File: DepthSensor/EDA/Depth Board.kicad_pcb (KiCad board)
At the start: 2 copper layers, 24 x 11.2 mm, 14 parts, among them J1 Conn_01x04, J2 Conn_01x03, J3 Screw_Terminal_01x03, J4 Conn_01x02, U1 ATmega328P-AU, Y1 8MHz

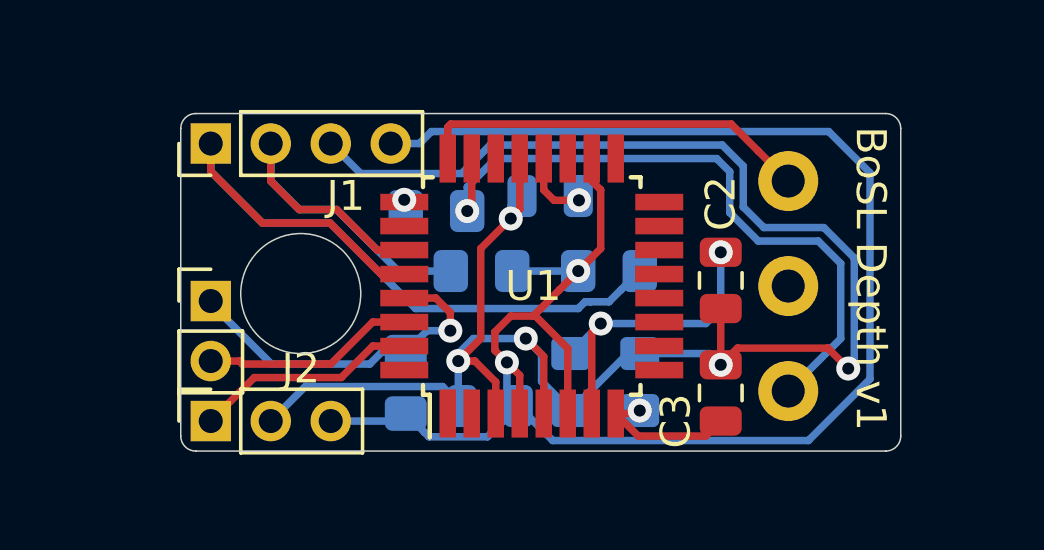
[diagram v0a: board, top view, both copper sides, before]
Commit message: added implementation of RS485 library
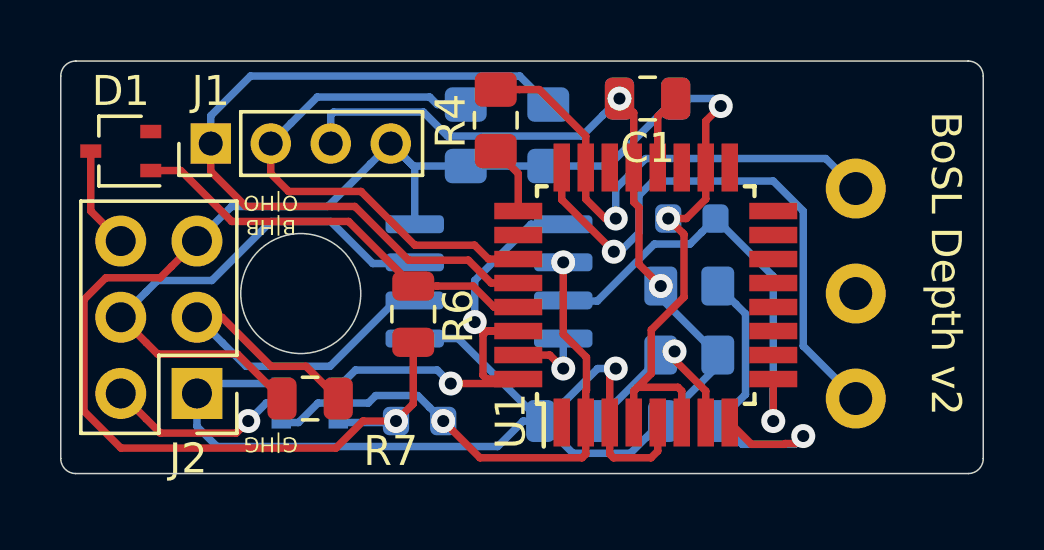
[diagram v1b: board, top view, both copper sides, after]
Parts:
- removed J4: Conn_01x02, SamacSys_Parts:Cable_2
- added D1: BAT54W, Package_TO_SOT_SMD:SOT-323_SC-70, F.Cu at (143.8, 95.0)
- added R5: 47 kΩ, Resistor_SMD:R_0603_1608Metric, B.Cu at (153.7, 104.0)
- added R6: 10 kΩ, Resistor_SMD:R_0805_2012Metric, F.Cu at (153.5, 100.4)
- added R7: 100 Ω, Resistor_SMD:R_0805_2012Metric, F.Cu at (150.1, 103.2)
- added U2: 74LVC1G126, Package_TO_SOT_SMD:SOT-353_SC-70-5, B.Cu at (150.1, 103.4)
- added U3: SN65HVD75, Package_SO:SOIC-8_3.9x4.9mm_P1.27mm, B.Cu at (156.0, 99.3)
- C1, R4: moved to F.Cu
- C2, C3: moved to B.Cu
- J2: value Conn_01x03 -> Conn_02x03_Odd_Even; footprint SamacSys_Parts:Cable -> Connector_PinHeader_2.54mm:PinHeader_2x03_P2.54mm_Vertical
- R1: value 10K -> 1 MΩ; footprint Resistor_SMD:R_0805_2012Metric_Pad1.15x1.40mm_HandSolder -> Resistor_SMD:R_0603_1608Metric
- moved C4 11.5 mm to (161.3, 93.2)
- moved R1 11.0 mm to (162.8, 97.2), turned to 180 degrees
- moved C2 6.90 mm to (158.7, 104.0), turned to 0 degrees
- moved R3 4.96 mm to (158.0, 94.5), turned to 90 degrees
- moved C1 4.60 mm to (161.3, 93.2)
- moved R2 4.56 mm to (155.2, 94.5), turned to 90 degrees
- moved U1 3.81 mm to (161.2, 99.8)
- moved R4 3.61 mm to (156.2, 94.0), turned to 90 degrees
- moved Y1 3.47 mm to (162.7, 100.7), turned to 270 degrees
- moved J3 2.26 mm to (168.2, 99.8), turned to 270 degrees
- moved C3 1.37 mm to (162.8, 104.0), turned to 180 degrees
- moved J2 1.03 mm to (146.3, 103.1), turned to 180 degrees
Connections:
- C1 pad 2: GND -> GREEN
- C2 pad 1: GND -> GREEN
- C3 pad 2: GND -> GREEN
- C4 pad 1: +3V3 -> ORANGE
- C4 pad 2: GND -> GREEN
- J1 pad 3: GND -> GREEN
- J1 pad 4: +3V3 -> ORANGE
- J2 pad 1: TX -> GREEN
- J2 pad 2: GND -> H_GREEN
- J2 pad 3: +3V3 -> BLUE
- R1 pad 1: +3V3 -> DE
- R1 pad 2: RST -> ORANGE
- R2 pad 1: +3V3 -> ORANGE
- R3 pad 1: +3V3 -> ORANGE
- U1 pad 18: +3V3 -> ORANGE
- U1 pad 2: (no net) -> RE
- U1 pad 21: GND -> GREEN
- U1 pad 29: RST -> Net-(D1-Pad1)
- U1 pad 3: GND -> GREEN
- U1 pad 30: RX -> Net-(U1-Pad30)
- U1 pad 31: TX -> Net-(U1-Pad31)
- U1 pad 32: (no net) -> Net-(U1-Pad30)
- U1 pad 4: +3V3 -> ORANGE
- U1 pad 5: GND -> GREEN
- U1 pad 6: +3V3 -> ORANGE
- U1 pad 9: (no net) -> DE
- Y1 pad 2: GND -> GREEN
- Y1 pad 3: GND -> GREEN
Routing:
- net GND: track 65.2 -> 0.00 mm, vias 5 -> 0
- net ORANGE: track 0.00 -> 62.8 mm, vias 0 -> 3
- net +3V3: track 62.2 -> 0.00 mm, vias 2 -> 0
- net GREEN: track 0.00 -> 59.2 mm, vias 0 -> 3
- net H_BLUE: track 0.00 -> 18.2 mm
- net RE: track 0.00 -> 18.2 mm, vias 0 -> 2
- net Net-(U1-Pad30): track 0.00 -> 16.9 mm, vias 0 -> 2
- net DE: track 0.00 -> 15.2 mm, vias 0 -> 1
- net BLUE: track 0.00 -> 14.7 mm
- net Net-(D1-Pad1): track 0.00 -> 14.1 mm
- net RST: track 11.7 -> 0.00 mm, vias 1 -> 0
- net TX: track 7.49 -> 0.00 mm
- net RX: track 7.07 -> 0.00 mm
- net Net-(C3-Pad1): track 4.86 -> 11.4 mm
- net H_GREEN: track 0.00 -> 6.31 mm, vias 0 -> 1
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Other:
- board size 24 x 11.2 mm -> 30.8 x 13.8 mm
- net class Default: clearance 0.2 -> 0.25
- rule trace_clearance: 0.2 -> 0.25
- board text added: "BoSL Depth v2"
- board text added: "G|HG B|HB O|HO"
- board text removed: "BoSL Depth v1"
